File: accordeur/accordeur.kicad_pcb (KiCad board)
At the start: 2 copper layers, 100 x 80 mm, 84 parts, among them J1 Screw_Terminal_01x03, Q1 2N3904, SW1 SW_SPST, U1 LM358, U10 LM358, U11 LM358, U2 LM358, U3 LM339, U4 LM358, U5 LM358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

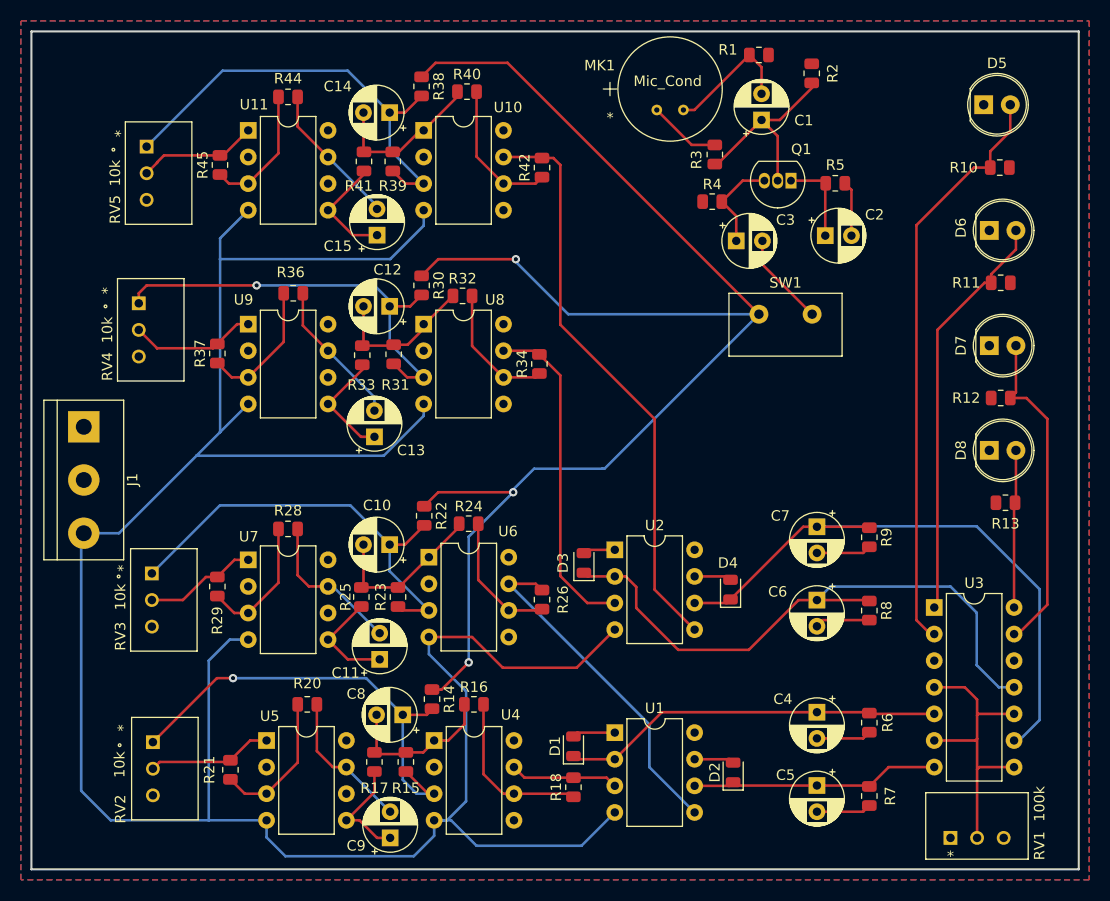
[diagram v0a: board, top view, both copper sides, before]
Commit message: Finalisation du placement des pièces
Prochaine étape : routing
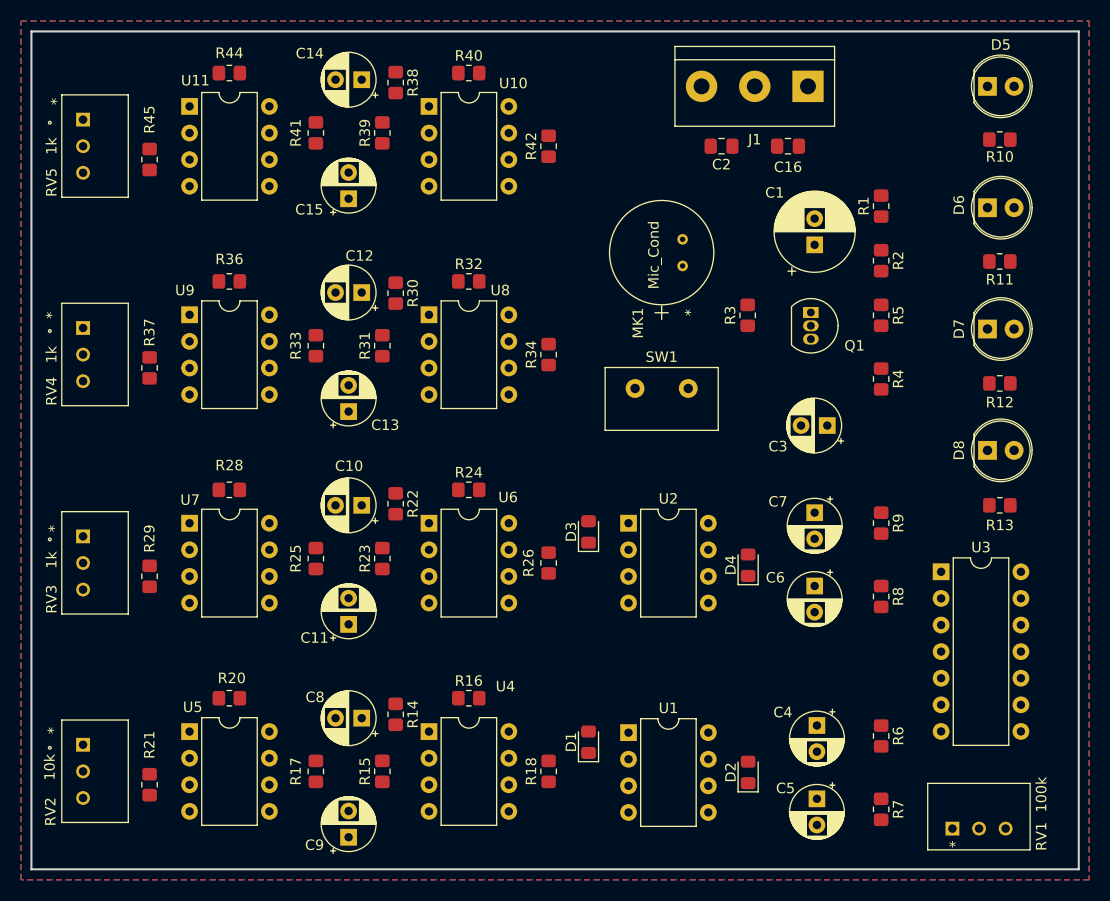
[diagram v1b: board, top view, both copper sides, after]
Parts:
- added C16: 100n, Capacitor_SMD:C_0805_2012Metric_Pad1.18x1.45mm_HandSolder, F.Cu at (142.2, 61.0)
- C1: value 1u -> 470u; footprint Capacitor_THT:CP_Radial_D5.0mm_P2.50mm -> Capacitor_THT:CP_Radial_D7.5mm_P2.50mm
- C2: value 1u -> 100n; footprint Capacitor_THT:CP_Radial_D5.0mm_P2.50mm -> Capacitor_SMD:C_0805_2012Metric_Pad1.18x1.45mm_HandSolder
- C3: value 1u -> 47u
- D1, D2, D3, D4: footprint Diode_SMD:D_0805_2012Metric -> Diode_SMD:D_0805_2012Metric_Pad1.15x1.40mm_HandSolder
- R1, R10, R11, R12, R13, R15, R20, R21, R23, R28, R29, R31, R36, R37, R39, R44, R45, R6, R7, R8, R9: footprint Resistor_SMD:R_0805_2012Metric -> Resistor_SMD:R_0805_2012Metric_Pad1.20x1.40mm_HandSolder
- R14, R22, R30, R38: value 51k -> 1,22k; footprint Resistor_SMD:R_0805_2012Metric -> Resistor_SMD:R_0805_2012Metric_Pad1.20x1.40mm_HandSolder
- R16, R2, R24, R32, R40: value R -> 1k; footprint Resistor_SMD:R_0805_2012Metric -> Resistor_SMD:R_0805_2012Metric_Pad1.20x1.40mm_HandSolder
- R17, R25, R33, R41: value 1,6k -> 1k; footprint Resistor_SMD:R_0805_2012Metric -> Resistor_SMD:R_0805_2012Metric_Pad1.20x1.40mm_HandSolder
- R18, R26: value R -> 4,3k; footprint Resistor_SMD:R_0805_2012Metric -> Resistor_SMD:R_0805_2012Metric_Pad1.20x1.40mm_HandSolder
- R3: value R -> 9,1k; footprint Resistor_SMD:R_0805_2012Metric -> Resistor_SMD:R_0805_2012Metric_Pad1.20x1.40mm_HandSolder
- R34: value R -> 8,2k; footprint Resistor_SMD:R_0805_2012Metric -> Resistor_SMD:R_0805_2012Metric_Pad1.20x1.40mm_HandSolder
- R4: value R -> 2,2k; footprint Resistor_SMD:R_0805_2012Metric -> Resistor_SMD:R_0805_2012Metric_Pad1.20x1.40mm_HandSolder
- R42: value R -> 10k; footprint Resistor_SMD:R_0805_2012Metric -> Resistor_SMD:R_0805_2012Metric_Pad1.20x1.40mm_HandSolder
- R5: value R -> 100; footprint Resistor_SMD:R_0805_2012Metric -> Resistor_SMD:R_0805_2012Metric_Pad1.20x1.40mm_HandSolder
- RV3, RV4, RV5: value 10k -> 1k
- moved J1 76.4 mm to (144.1, 55.2), turned to 180 degrees
- moved R4 23.4 mm to (151.1, 83.2), turned to -90 degrees
- moved C3 19.7 mm to (146.0, 87.6), turned to 180 degrees
- moved R2 19.1 mm to (151.1, 71.9)
- moved R1 18.6 mm to (151.1, 66.7), turned to 90 degrees
- moved MK1 16.9 mm to (130.2, 72.4), turned to 90 degrees
- moved R3 15.7 mm to (138.4, 77.1)
- moved SW1 13.8 mm to (130.2, 85.1)
- moved R5 13.3 mm to (151.1, 77.1), turned to -90 degrees
- moved C2 13.1 mm to (135.9, 61.0)
- moved C1 13.0 mm to (144.8, 70.4)
- moved Q1 12.7 mm to (144.4, 76.8), turned to -90 degrees
- moved R21 7.85 mm to (81.3, 121.9)
- moved RV3 7.46 mm to (74.9, 98.2)
- moved R20 7.46 mm to (88.9, 113.7)
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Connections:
- C2 pad 1: Net-(C2-Pad1) -> -5V
- Q1 pad 1: Net-(C2-Pad1) -> Net-(Q1-Pad1)
- R5 pad 1: Net-(C2-Pad1) -> Net-(Q1-Pad1)
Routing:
- net -5V: track 234.8 -> 0.00 mm
- net /PB A3/v_sig: track 140.2 -> 0.00 mm, vias 3 -> 0
- net Net-(C6-Pad1): track 59.7 -> 0.00 mm
- net Net-(C7-Pad1): track 59.2 -> 0.00 mm
- net Net-(D5-Pad2): track 56.1 -> 0.00 mm
- net /PB Fd4/v_PB_Fd4: track 55.4 -> 0.00 mm
- net Net-(C8-Pad1): track 44.3 -> 0.00 mm, vias 1 -> 0
- net Net-(C14-Pad1): track 43.1 -> 0.00 mm
- net Net-(C10-Pad1): track 41.9 -> 0.00 mm
- net Net-(C12-Pad1): track 40.8 -> 0.00 mm, vias 1 -> 0
- net Net-(D6-Pad2): track 39.6 -> 0.00 mm
- net Net-(C4-Pad1): track 36.5 -> 0.00 mm
- net GND: track 33.2 -> 0.00 mm
- net /PB A3/v_PB_A3: track 32.6 -> 0.00 mm
- net /PB C4/v_PB_C4: track 31.8 -> 0.00 mm
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
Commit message: PCB commandé
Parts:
- moved C7 7.05 mm to (145.0, 103.0)
- moved R9 7.05 mm to (151.1, 104.0)
- moved C6 7.00 mm to (145.0, 95.9)
- moved R8 7.00 mm to (151.1, 96.9)
- turned R10 to 0 degrees
- turned R11 to 0 degrees
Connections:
- R3 pad 2: GND -> -5V
- R5 pad 2: GND -> -5V
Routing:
- net -5V: track 0.00 -> 288.0 mm, vias 0 -> 2
- net /PB A3/v_sig: track 0.00 -> 103.7 mm
- net Net-(D5-Pad2): track 0.00 -> 58.6 mm
- net /PB Fd4/v_PB_Fd4: track 0.00 -> 54.8 mm
- net Net-(C6-Pad1): track 0.00 -> 53.9 mm
- net Net-(C14-Pad1): track 0.00 -> 49.2 mm
- net Net-(C12-Pad1): track 0.00 -> 48.8 mm
- net Net-(C10-Pad1): track 0.00 -> 48.0 mm
- net Net-(C8-Pad1): track 0.00 -> 47.3 mm
- net Net-(C7-Pad1): track 0.00 -> 43.4 mm
- net Net-(D6-Pad2): track 0.00 -> 42.9 mm
- net Net-(C4-Pad1): track 0.00 -> 38.2 mm
- net GND: track 0.00 -> 36.7 mm
- net /PB A3/v_PB_A3: track 0.00 -> 35.0 mm
- net v_ref: track 0.00 -> 34.8 mm
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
